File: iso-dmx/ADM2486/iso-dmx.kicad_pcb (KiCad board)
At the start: 2 copper layers, 19 x 23.5 mm, 12 parts, among them J1 Conn_01x06, J2 Conn_01x06, U1 ADM809-5SARTZ-RL7, U2 TME-0305S, U3 ADM2486

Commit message: A6211 Basic Layout
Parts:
- moved JP3 0.64 mm to (83.8, 64.1)
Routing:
- net GND1: track 9.29 -> 8.42 mm, vias 10 -> 9
- net GND2: vias 9 -> 11
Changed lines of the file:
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@@
 			(solder_mask_margin 0.102)
+		)
+		(model "${KIPRJMOD}/footprints/ADM809-5SARTZ-RL7.step"
+			(offset
+				(xyz 0 0 0)
+			)
+			(scale
+				(xyz 1 1 1)
+			)
+			(rotate
+				(xyz -90 0 0)
+			)
 		)
 	)
@@
 	(footprint "Jumper:SolderJumper-2_P1.3mm_Open_Pad1.0x1.5mm"
 		(layer "B.Cu")
-		(at 83.82 63.5)
+		(at 83.82 64.135)
 		(descr "SMD Solder Jumper, 1x1.5mm Pads, 0.3mm gap, open")
 		(tags "solder jumper open")
@@
 	)
 	(gr_text "DE"
-		(at 81.788 59.055 0)
+		(at 80.772 59.055 0)
 		(layer "B.SilkS")
 		(effects
@@
 				(thickness 0.1)
 			)
-			(justify mirror)
+			(justify right mirror)
 		)
 	)
 	(gr_text "GND2"
-		(at 85.4964 63.5 0)
+		(at 84.455 62.484 0)
 		(layer "B.SilkS")
 		(effects
@@
 	)
 	(gr_text "GND1"
-		(at 82.1944 63.5 0)
+		(at 83.185 62.484 0)
 		(layer "B.SilkS")
 		(effects
@@
 	)
 	(gr_text "NRE"
-		(at 81.788 57.785 0)
+		(at 80.772 57.785 0)
 		(layer "B.SilkS")
 		(effects
@@
 				(thickness 0.1)
 			)
-			(justify mirror)
+			(justify right mirror)
 		)
 	)
@@
 	)
 	(via
+		(at 85.721 58.355)
+		(size 0.7)
+		(drill 0.3)
+		(layers "F.Cu" "B.Cu")
+		(free yes)
+		(net 2)
+	)
+	(via
+		(at 86.487 61.214)
+		(size 0.7)
+		(drill 0.3)
+		(layers "F.Cu" "B.Cu")
+		(free yes)
+		(net 2)
+	)
+	(via
 		(at 92.075 48.641)
 		(size 0.7)
@@
 	)
 	(via
-		(at 81.407 62.484)
-		(size 0.7)
-		(drill 0.3)
-		(layers "F.Cu" "B.Cu")
-		(free yes)
-		(net 4)
-	)
-	(via
 		(at 75.565 47.371)
 		(size 0.7)
@@
 	)
 	(segment
-		(start 83.17 62.096)
-		(end 83.17 63.5)
+		(start 83.671 61.595)
+		(end 82.423 61.595)
 		(width 0.4)
 		(layer "B.Cu")
@@
 	(segment
 		(start 85.161 60.105)
-		(end 83.17 62.096)
-		(width 0.4)
-		(layer "B.Cu")
+		(end 83.671 61.595)
+		(width 0.4)
+		(layer "B.Cu")

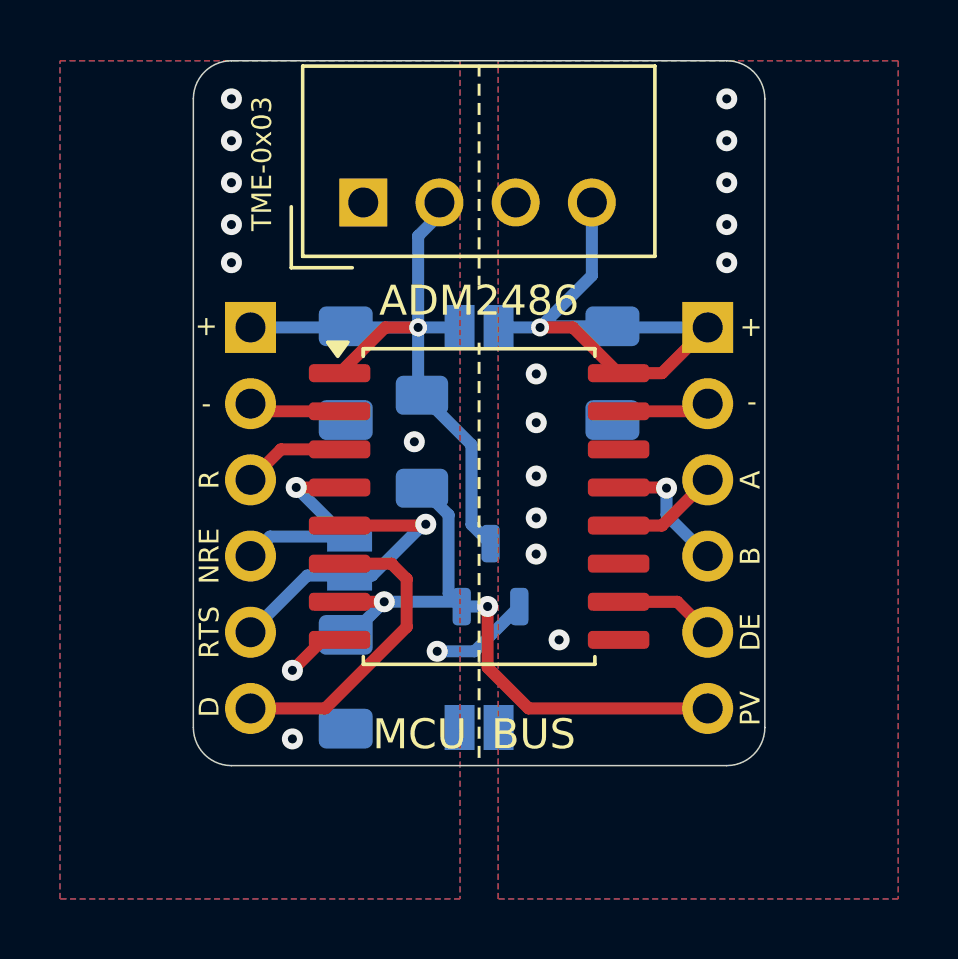
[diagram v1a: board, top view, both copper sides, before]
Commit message: ISO DMX Logos
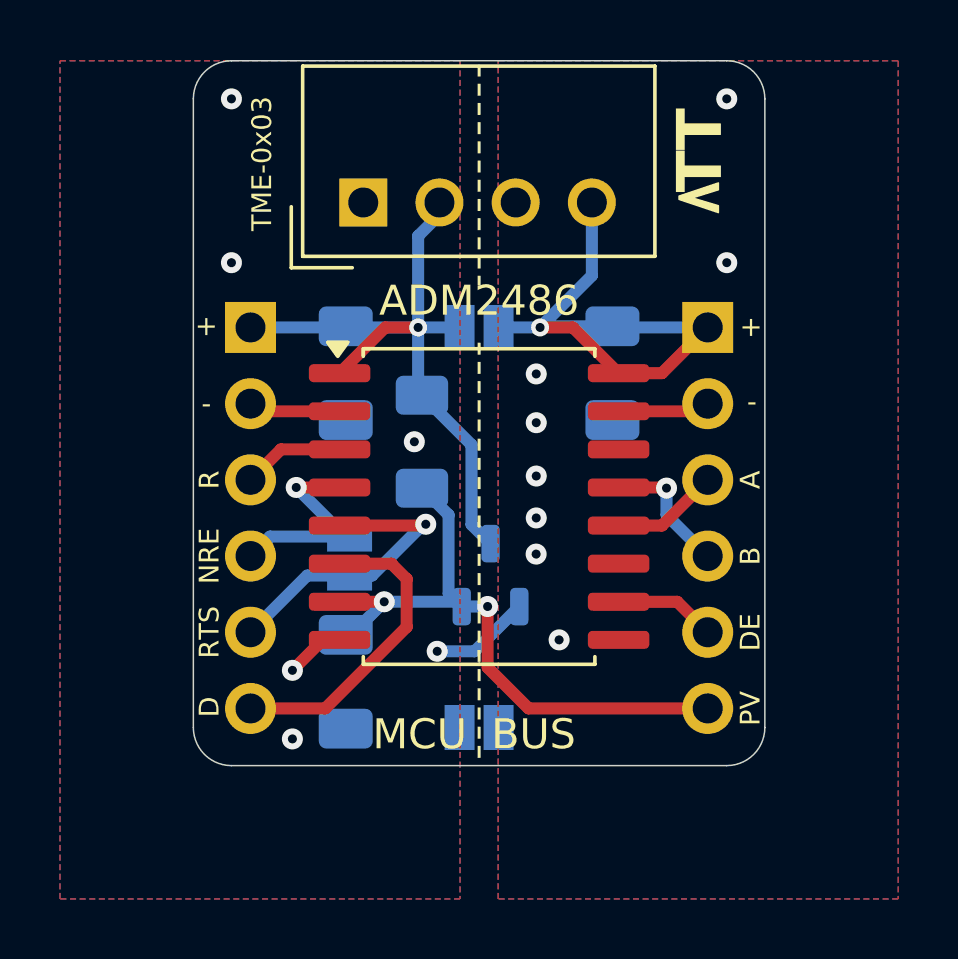
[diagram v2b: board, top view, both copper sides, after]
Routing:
- net GND2: vias 11 -> 8
- net GND1: vias 9 -> 6
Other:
- board text added: "TT"
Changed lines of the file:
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@@
+		(layer "B.SilkS")
+	)
+	(gr_poly
+		(pts
+			(xy 84.402 44.044001) (xy 84.841999 42.734) (xy 84.951999 42.734) (xy 85.391999 44.044) (xy 85.161999 44.044001)
+			(xy 84.901999 43.173999) (xy 84.632 44.043999)
+		)
+		(stroke
+			(width 0.05)
+			(type solid)
+		)
+		(fill solid)
 		(layer "B.SilkS")
 	)
@@
 			(type dot)
 		)
+		(layer "F.SilkS")
+	)
+	(gr_poly
+		(pts
+			(xy 91.796001 45.982) (xy 90.486 46.422) (xy 90.486 46.532) (xy 91.796 46.972) (xy 91.796001 46.742)
+			(xy 90.926 46.482) (xy 91.796 46.212)
+		)
+		(stroke
+			(width 0.05)
+			(type solid)
+		)
+		(fill solid)
 		(layer "F.SilkS")
 	)
@@
 		(layer "Edge.Cuts")
 	)
+	(gr_text "TT"
+		(at 83.312 43.434 0)
+		(layer "B.SilkS")
+		(effects
+			(font
+				(face "Inconsolata")
+				(size 1.5 1.5)
+				(thickness 0.3)
+				(bold yes)
+			)
+			(justify mirror)
+		)
+		(render_cache "TT" 0
+			(polygon
+				(pts
+					(xy 83.958266 44.0565) (xy 83.958266 42.943851) (xy 84.312906 42.943851) (xy 84.312906 42.74345)
+					(xy 83.356696 42.74345) (xy 83.356696 42.943851) (xy 83.730387 42.943851) (xy 83.730387 44.0565)
+				)
+			)
+			(polygon
+				(pts
+					(xy 82.908999 44.0565) (xy 82.908999 42.943851) (xy 83.263639 42.943851) (xy 83.263639 42.74345)
+					(xy 82.307428 42.74345) (xy 82.307428 42.943851) (xy 82.68112 42.943851) (xy 82.68112 44.0565)
+				)
+			)
+		)
+	)
 	(gr_text "DE"
 		(at 80.772 59.055 0)
@@
 		)
 	)
+	(gr_text "TT"
+		(at 91.186 44.892 90)
+		(layer "F.SilkS")
+		(effects
+			(font
+				(face "Inconsolata")
+				(size 1.5 1.5)
+				(thickness 0.3)
+				(bold yes)
+			)
+		)
+		(render_cache "TT" 90
+			(polygon
+				(pts
+					(xy 91.8085 45.538266) (xy 90.695851 45.538266) (xy 90.695851 45.892906) (xy 90.49545 45.892906)
+					(xy 90.49545 44.936696) (xy 90.695851 44.936696) (xy 90.695851 45.310387) (xy 91.8085 45.310387)
+				)
+			)
+			(polygon
+				(pts
+					(xy 91.8085 44.488999) (xy 90.695851 44.488999) (xy 90.695851 44.843639) (xy 90.49545 44.843639)
+					(xy 90.49545 43.887428) (xy 90.695851 43.887428) (xy 90.695851 44.26112) (xy 91.8085 44.26112)
+				)
+			)
+		)
+	)
 	(gr_text "B"
 		(at 92.8624 58.42 90)
@@
 	)
 	(via
-		(at 92.075 44.577)
-		(size 0.7)
-		(drill 0.3)
-		(layers "F.Cu" "B.Cu")
-		(free yes)
-		(net 2)
-	)
-	(via
 		(at 85.725 57.15)
 		(size 0.7)
@@
 	(via
 		(at 85.725 53.975)
-		(size 0.7)
-		(drill 0.3)
-		(layers "F.Cu" "B.Cu")
-		(free yes)
-		(net 2)
-	)
-	(via
-		(at 92.075 45.974)
-		(size 0.7)
-		(drill 0.3)
-		(layers "F.Cu" "B.Cu")
-		(free yes)
-		(net 2)
-	)
-	(via
-		(at 92.075 47.371)
 		(size 0.7)
 		(drill 0.3)
@@
 	)
 	(via
-		(at 75.565 47.371)
-		(size 0.7)
-		(drill 0.3)
-		(layers "F.Cu" "B.Cu")
-		(free yes)
-		(net 4)
-	)
-	(via
 		(at 82.423 61.595)
 		(size 0.7)
 		(drill 0.3)
-		(layers "F.Cu" "B.Cu")
-		(free yes)
-		(net 4)
-	)
-	(via
-		(at 75.565 44.577)
-		(size 0.7)
-		(drill 0.3)
-		(layers "F.Cu" "B.Cu")
-		(free yes)
-		(net 4)
-	)
-	(via
-		(at 75.565 45.974)
-		(size 0.7)
-		(drill 0.3)
